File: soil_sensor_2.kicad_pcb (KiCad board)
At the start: 2 copper layers, 26 x 150 mm, 27 parts, among them J1 ESP-PROG, Q1 SI2312, U1 HDC1080, U2 TPS61201DRCT, U3 ESP32-PICO-V3

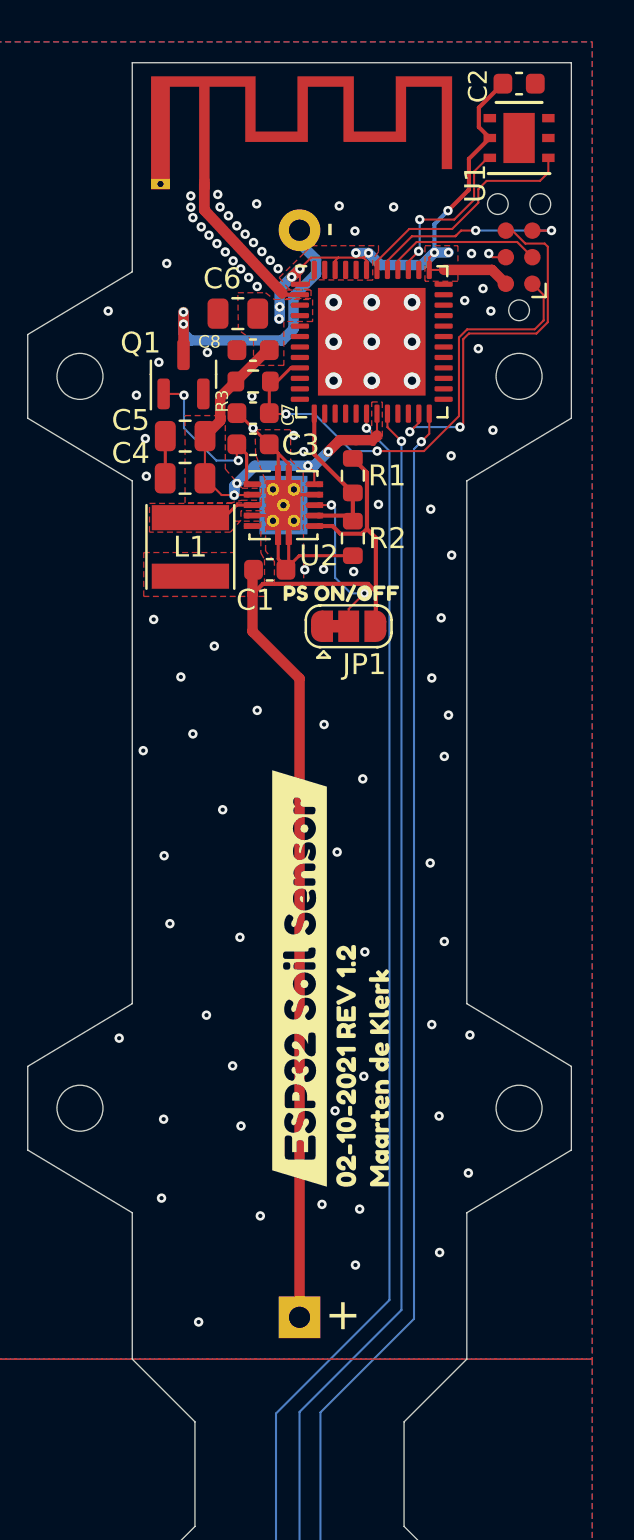
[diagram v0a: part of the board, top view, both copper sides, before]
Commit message: update BMS
now using the TPS61201DRCT
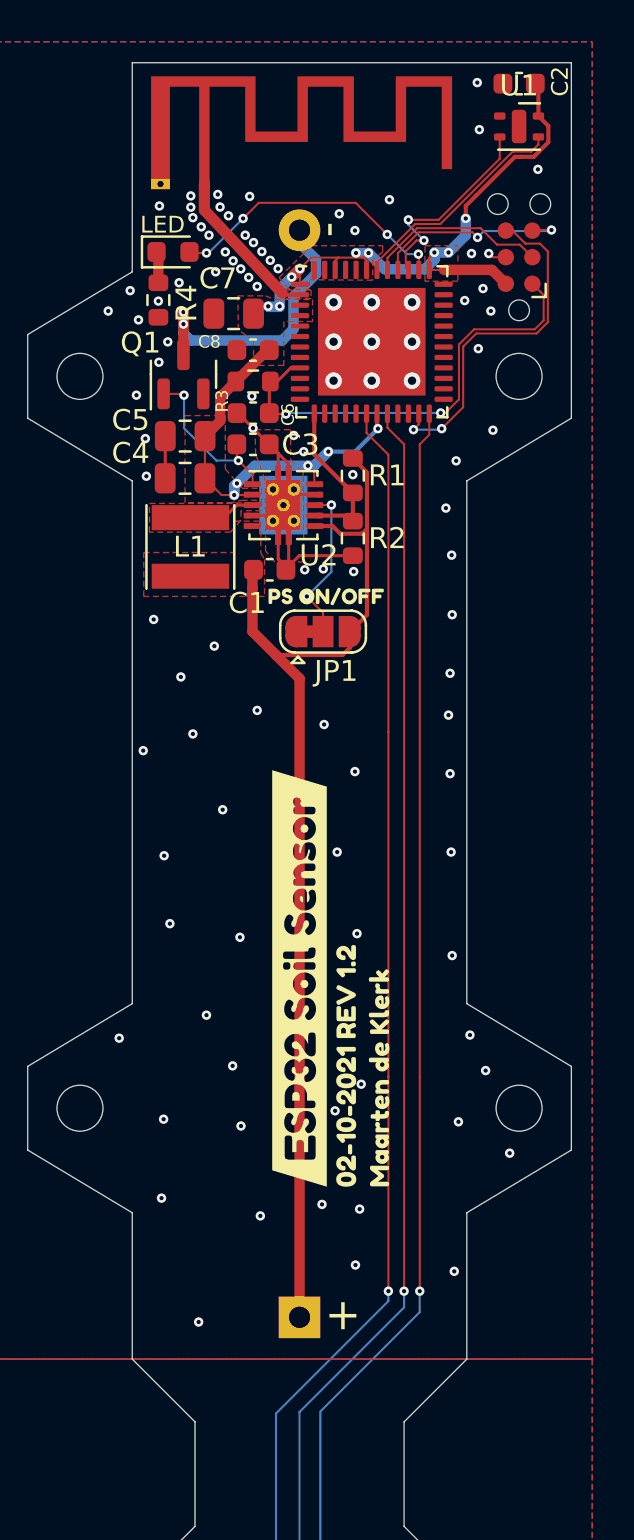
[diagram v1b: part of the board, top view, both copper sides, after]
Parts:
- added D1: LED, LED_SMD:LED_0603_1608Metric, F.Cu at (98.0, 64.0)
- added R4: 3k3, Resistor_SMD:R_0603_1608Metric, F.Cu at (97.2, 66.3)
- R1: value 2.87M -> 2M
- U1: value HDC1080 -> SHT40; footprint Package_SON:Texas_PWSON-N6 -> Sensor_Humidity:Sensirion_DFN-4-1EP_2x2mm_P1mm_EP0.7x1.6mm
- moved JP1 1.25 mm to (105.1, 82.2)
- moved kibuzzard-61586E44 0.74 mm to (105.3, 80.5)
- moved U1 0.55 mm to (114.5, 58.0), turned to 0 degrees
- moved C7 0.20 mm to (100.8, 67.0)
- turned C2 to 180 degrees
- renumbered C7 to C6, C6 to C7
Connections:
- U1 pad 1: /SDA -> GND
- U1 pad 2: GND -> /SCL
- U1 pad 3: unconnected-(U1-Pad3) -> /SDA
- U1 pad 4: unconnected-(U1-Pad4) -> +3V3
- U1 pad 5: +3V3 -> unconnected-(U1-Pad5)
- U3 pad 38: unconnected-(U3-Pad38) -> Net-(D1-Pad2)
- U3 pad 40: /TXD -> /RXD
- U3 pad 41: /RXD -> /TXD
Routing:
- net Net-(D1-Pad2): track 0.00 -> 13.7 mm, vias 0 -> 4
- net /EN: track 23.9 -> 21.7 mm
- net /SCL: track 8.00 -> 9.94 mm
- net Net-(D1-Pad1): track 0.00 -> 1.51 mm
- net /BAT+: track 54.2 -> 52.8 mm
- net /BOOT: track 18.1 -> 16.9 mm
- net +3V3: track 49.5 -> 50.7 mm, vias 13 -> 14
- net /TXD: track 7.54 -> 8.67 mm
- net Net-(C3-Pad1): track 8.72 -> 8.04 mm
- net /SDA: track 11.4 -> 10.8 mm
- net Net-(JP1-Pad2): track 7.97 -> 7.40 mm
- net GND: vias 96 -> 102
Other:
- board text added: "LED"
